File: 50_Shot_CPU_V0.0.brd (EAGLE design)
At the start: 86 x 100 mm, 76 parts, among them IC1 PIC24FJ128GA010, IC2 93LC46ST, J1 J12, J12 A311422_nd, J13 22-23-2021, J14 22-23-2021, J3 22-23-2021, J4 22-23-2021, J5 22-23-2021, Q1 Qs5U34CT-ND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

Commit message: Removed 5V reg and parts
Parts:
- removed C19: 0.01uF, rcl:C0805
- removed C21: 10uF, Mine:CAP3X3
- removed F1: 5A, Mine:SH22,5A
- removed U4: MIC29300, linear:TO263-3
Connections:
- removed net N$60: C21.+, F1.1, U4.3
- removed net VCC: F1.2
- net +12V: no longer C19.1, U4.1
- net GND: no longer C19.2, C21.-, U4.2
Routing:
- net N$60: track 54.7 -> 0.00 mm, vias 1 -> 0
- net VCC: track 37.0 -> 0.00 mm
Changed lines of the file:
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@@
 <attribute name="NAME" x="33.918" y="24.98" size="1.27" layer="25"/>
-</element>
-<element name="C19" library="rcl" package="C0805" value="0.01uF" x="42.178" y="47.836" smashed="yes" rot="R90">
-<attribute name="NAME" x="44.62" y="45.226" size="1.27" layer="25" rot="R180"/>
-</element>
-<element name="C21" library="Mine" package="CAP3X3" value="10uF" x="72.17" y="55.432" smashed="yes" rot="R90">
-<attribute name="NAME" x="73.727" y="52.612" size="1.27" layer="25" rot="R180"/>
 </element>
 <element name="C10" library="rcl" package="C0805" value="10nF" x="57.112" y="48.858" smashed="yes" rot="R180">
@@
 <element name="D3" library="adafruit" package="SOD-123" value="641-1014-6-ND" x="61.38" y="92.82" smashed="yes">
 <attribute name="NAME" x="60.026" y="94.074" size="1.27" layer="25"/>
-</element>
-<element name="F1" library="Mine" package="SH22,5A" value="5A" x="56.368" y="67.79" smashed="yes" rot="R180">
-<attribute name="NAME" x="43.16" y="68.806" size="1.6764" layer="25" ratio="10" rot="R180"/>
-<attribute name="VALUE" x="43.3886" y="65.758" size="1.4224" layer="27" ratio="10" rot="R180"/>
 </element>
 <element name="IC1" library="microchip" package="TQFP100-14X14" value="PIC24FJ128GA010" x="26.79" y="59.89" smashed="yes" rot="R180">
@@
 <attribute name="OC_NEWARK" value="79K3928" x="52.224" y="19.8" size="1.778" layer="27" display="off"/>
 <attribute name="NAME" x="48.5156" y="20.054" size="1.27" layer="25" ratio="10" rot="SR0"/>
-</element>
-<element name="U4" library="linear" package="TO263-3" value="MIC29300" x="66.31" y="34.938" smashed="yes">
-<attribute name="NAME" x="59.804" y="41.926" size="1.27" layer="25" rot="R180"/>
 </element>
 <element name="U1" library="Mine" package="SSOP20" value="MAX6818" x="25.66" y="27.716" smashed="yes" rot="R270">
@@
 <signal name="+12V">
 <contactref element="R1" pad="2"/>
-<contactref element="C19" pad="1"/>
-<contactref element="U4" pad="1"/>
 <contactref element="U2" pad="3"/>
 <contactref element="U2" pad="1"/>
@@
 <wire x1="45.72" y1="46.89" x2="45.71" y2="46.9" width="0.254" layer="1"/>
 <wire x1="45.71" y1="46.9" x2="42.192" y2="46.9" width="0.254" layer="1"/>
-<wire x1="42.192" y1="46.9" x2="42.178" y2="46.886" width="0.254" layer="1"/>
 <wire x1="50.9286" y1="18.8602" x2="49.9738" y2="18.8602" width="0.254" layer="1"/>
 <wire x1="49.9738" y1="18.8602" x2="49.53" y2="19.304" width="0.254" layer="1"/>
@@
 <wire x1="58.674" y1="22.352" x2="53.594" y2="22.352" width="0.254" layer="1"/>
 <wire x1="53.594" y1="22.352" x2="48.006" y2="27.94" width="0.254" layer="1"/>
-<wire x1="63.77" y1="29.1468" x2="63.7068" y2="29.21" width="0.4064" layer="1"/>
 <wire x1="63.7068" y1="29.21" x2="62.23" y2="29.21" width="0.4064" layer="1"/>
 <via x="62.23" y="29.21" extent="1-16" drill="0.6"/>
 <wire x1="46.228" y1="38.354" x2="44.45" y2="38.354" width="0.4064" layer="16"/>
-<wire x1="63.77" y1="29.1468" x2="63.688" y2="29.0648" width="0.254" layer="1"/>
 <wire x1="62.23" y1="29.21" x2="55.372" y2="29.21" width="0.4064" layer="16"/>
 <wire x1="55.372" y1="29.21" x2="46.228" y2="38.354" width="0.4064" layer="16"/>
@@
 <contactref element="C13" pad="2"/>
 <contactref element="C9" pad="2"/>
-<contactref element="C19" pad="2"/>
-<contactref element="C21" pad="-"/>
-<contactref element="U4" pad="2"/>
 <contactref element="U2" pad="2"/>
 <contactref element="U3" pad="2"/>
@@
 <contactref element="IC2" pad="5"/>
 <contactref element="C6" pad="2"/>
-<wire x1="2.064" y1="-46.99" x2="45.546" y2="-51.308" width="0" layer="19" extent="1-1"/>
-<wire x1="13.89" y1="-33.782" x2="2.064" y2="-46.99" width="0" layer="19" extent="1-1"/>
-<wire x1="27.686" y1="-19.05" x2="13.89" y2="-33.782" width="0" layer="19" extent="1-1"/>
-<wire x1="40.64" y1="-18.288" x2="27.686" y2="-19.05" width="0" layer="19" extent="1-1"/>
-<wire x1="52.324" y1="-17.78" x2="40.64" y2="-18.288" width="0" layer="19" extent="1-1"/>
-<wire x1="65.532" y1="-18.288" x2="52.324" y2="-17.78" width="0" layer="19" extent="1-1"/>
-<wire x1="77.216" y1="-18.542" x2="65.532" y2="-18.288" width="0" layer="19" extent="1-1"/>
+<wire x1="65.532" y1="-18.288" x2="77.216" y2="-18.542" width="0" layer="19" extent="1-1"/>
+<wire x1="52.324" y1="-17.78" x2="65.532" y2="-18.288" width="0" layer="19" extent="1-1"/>
+<wire x1="40.64" y1="-18.288" x2="52.324" y2="-17.78" width="0" layer="19" extent="1-1"/>
+<wire x1="27.686" y1="-19.05" x2="40.64" y2="-18.288" width="0" layer="19" extent="1-1"/>
 <wire x1="45.171" y1="-31.873" x2="40.64" y2="-18.288" width="0" layer="19" extent="1-1"/>
 <wire x1="50.988" y1="-35.56" x2="45.171" y2="-31.873" width="0" layer="19" extent="1-1"/>
+<wire x1="45.546" y1="-51.308" x2="50.988" y2="-35.56" width="0" layer="19" extent="1-1"/>
+<wire x1="13.89" y1="-33.782" x2="27.686" y2="-19.05" width="0" layer="19" extent="1-1"/>
+<wire x1="2.064" y1="-46.99" x2="13.89" y2="-33.782" width="0" layer="19" extent="1-1"/>
 <wire x1="80.07" y1="2.78" x2="77.216" y2="-18.542" width="0" layer="19" extent="1-1"/>
-</signal>
-<signal name="VCC">
-<contactref element="F1" pad="2"/>
-<wire x1="80.162" y1="72.39" x2="65.024" y2="72.39" width="0.4064" layer="16"/>
-<wire x1="65.024" y1="72.39" x2="60.424" y2="67.79" width="0.4064" layer="16"/>
-<wire x1="60.424" y1="67.79" x2="45.1158" y2="67.79" width="0.4064" layer="16"/>
 </signal>
 <signal name="VDD">
@@
 <wire x1="43.61" y1="79.932" x2="45.114" y2="79.932" width="0.254" layer="1"/>
 </signal>
-<signal name="N$60">
-<contactref element="C21" pad="+"/>
-<contactref element="U4" pad="3"/>
-<contactref element="F1" pad="1"/>
-<via x="70.866" y="29.21" extent="1-16" drill="0.6"/>
-<wire x1="72.17" y1="56.882" x2="72.136" y2="58.44" width="0.4064" layer="1"/>
-<wire x1="72.136" y1="58.44" x2="72.136" y2="63.2742" width="0.4064" layer="1"/>
-<wire x1="72.136" y1="63.2742" x2="67.6202" y2="67.79" width="0.4064" layer="1"/>
-<wire x1="68.85" y1="29.1468" x2="70.8028" y2="29.1468" width="0.4064" layer="1"/>
-<wire x1="70.8028" y1="29.1468" x2="70.866" y2="29.21" width="0.4064" layer="1"/>
-<wire x1="70.866" y1="29.21" x2="70.866" y2="39.878" width="0.4064" layer="16"/>
-<wire x1="70.866" y1="39.878" x2="67.6202" y2="43.1238" width="0.4064" layer="16"/>
-<wire x1="67.6202" y1="43.1238" x2="67.6202" y2="67.79" width="0.4064" layer="16"/>
-</signal>
 <signal name="ON_LED">

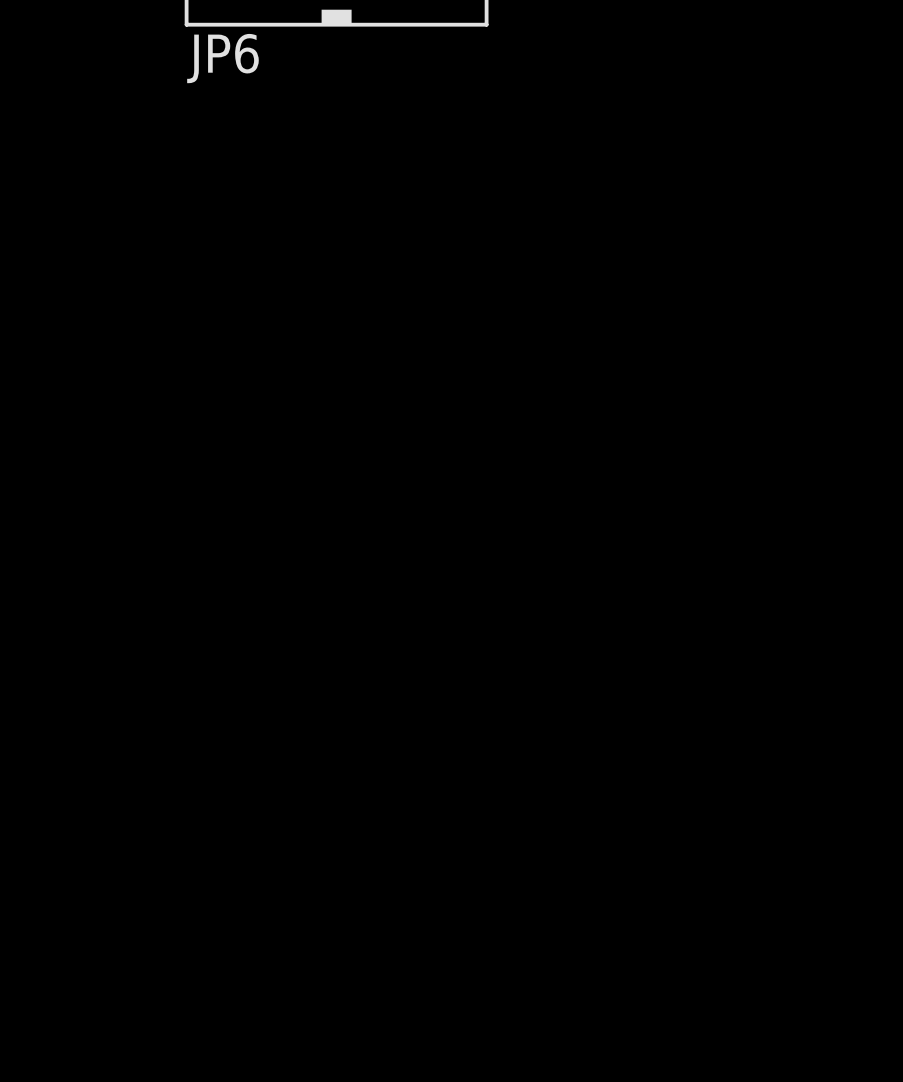
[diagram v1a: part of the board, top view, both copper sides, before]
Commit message: Added parallel display header
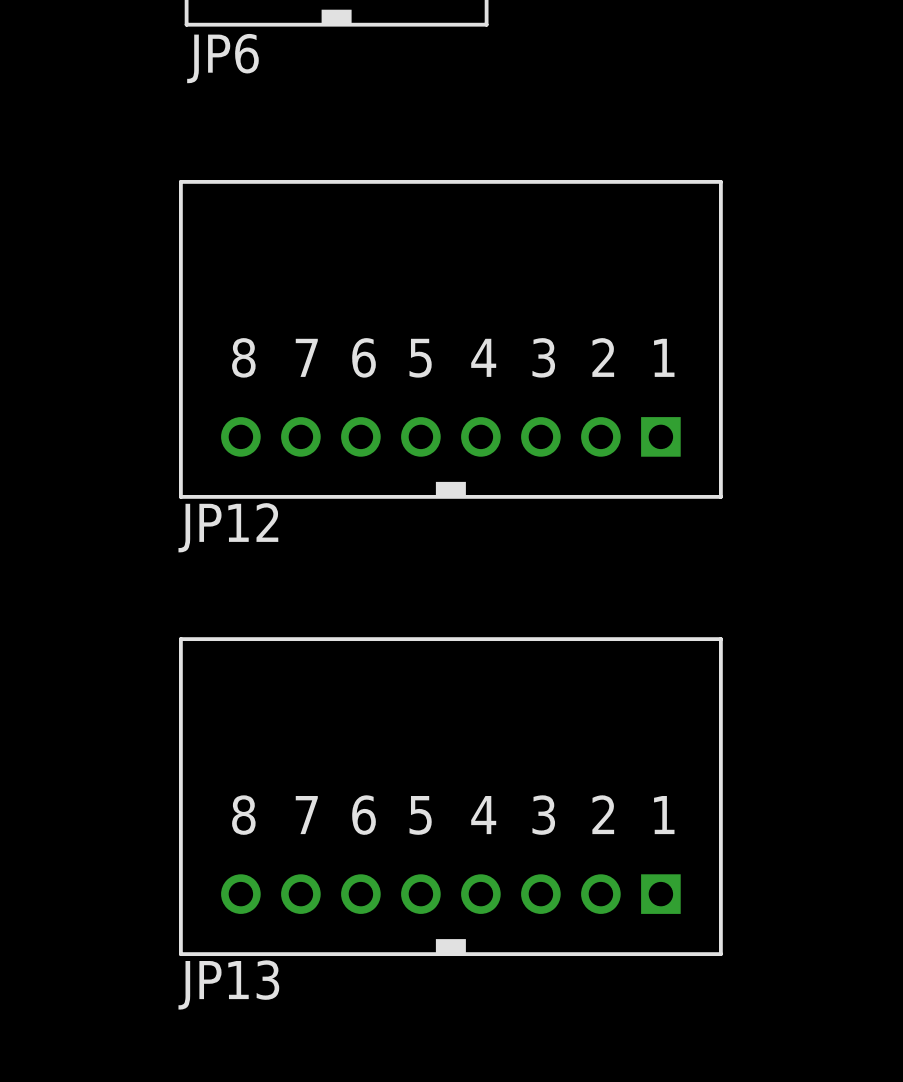
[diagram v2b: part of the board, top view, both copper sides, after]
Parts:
- added JP12, JP13: SHERLOCK_8PIN_RGT, Mine:SHERLOCK_8PIN-RGT
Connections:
- removed net RD10: IC1.70
- removed net RD11: IC1.71
- removed net RD12: IC1.79
- removed net RD13: IC1.80
- removed net RD14: IC1.47
- removed net RD2: IC1.77
- removed net RD3: IC1.78
- removed net RD4: IC1.81
- removed net RD5: IC1.82
- removed net RD6: IC1.83
- removed net RD7: IC1.84
- removed net RD8: IC1.68
- removed net RD9: IC1.69
- new net RD10_CS: IC1.70, JP12.3
- new net RD11_CD: IC1.71, JP12.4
- new net RD12_WR: IC1.79, JP12.5
- new net RD13_RD: IC1.80, JP12.6
- new net RD14_RST: IC1.47, JP12.7
- new net RD2_D0: IC1.77, JP13.1
- new net RD3_D1: IC1.78, JP13.2
- new net RD4_D2: IC1.81, JP13.3
- new net RD5_D3: IC1.82, JP13.4
- new net RD6_D4: IC1.83, JP13.5
- new net RD7_D5: IC1.84, JP13.6
- new net RD8_D6: IC1.68, JP13.7
- new net RD9_D7: IC1.69, JP13.8
- net GND: now also JP12.1
- net RD15: now also JP12.8
- net VDD: now also JP12.2
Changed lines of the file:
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@@
 </element>
 <element name="C6" library="rcl" package="C0805" value=".01uf" x="50.038" y="-35.56"/>
+<element name="JP12" library="Mine" package="SHERLOCK_8PIN-RGT" value="SHERLOCK_8PIN_RGT" x="8.89" y="-107.95"/>
+<element name="JP13" library="Mine" package="SHERLOCK_8PIN-RGT" value="SHERLOCK_8PIN_RGT" x="8.89" y="-123.19"/>
 </elements>
 <signals>
@@
 <contactref element="IC2" pad="5"/>
 <contactref element="C6" pad="2"/>
-<wire x1="65.532" y1="-18.288" x2="77.216" y2="-18.542" width="0" layer="19" extent="1-1"/>
-<wire x1="52.324" y1="-17.78" x2="65.532" y2="-18.288" width="0" layer="19" extent="1-1"/>
-<wire x1="40.64" y1="-18.288" x2="52.324" y2="-17.78" width="0" layer="19" extent="1-1"/>
-<wire x1="27.686" y1="-19.05" x2="40.64" y2="-18.288" width="0" layer="19" extent="1-1"/>
+<contactref element="JP12" pad="1"/>
+<wire x1="2.064" y1="-46.99" x2="15.89" y2="-107.95" width="0" layer="19" extent="1-1"/>
+<wire x1="13.89" y1="-33.782" x2="2.064" y2="-46.99" width="0" layer="19" extent="1-1"/>
+<wire x1="27.686" y1="-19.05" x2="13.89" y2="-33.782" width="0" layer="19" extent="1-1"/>
+<wire x1="40.64" y1="-18.288" x2="27.686" y2="-19.05" width="0" layer="19" extent="1-1"/>
+<wire x1="52.324" y1="-17.78" x2="40.64" y2="-18.288" width="0" layer="19" extent="1-1"/>
+<wire x1="65.532" y1="-18.288" x2="52.324" y2="-17.78" width="0" layer="19" extent="1-1"/>
+<wire x1="77.216" y1="-18.542" x2="65.532" y2="-18.288" width="0" layer="19" extent="1-1"/>
 <wire x1="45.171" y1="-31.873" x2="40.64" y2="-18.288" width="0" layer="19" extent="1-1"/>
 <wire x1="50.988" y1="-35.56" x2="45.171" y2="-31.873" width="0" layer="19" extent="1-1"/>
 <wire x1="45.546" y1="-51.308" x2="50.988" y2="-35.56" width="0" layer="19" extent="1-1"/>
-<wire x1="13.89" y1="-33.782" x2="27.686" y2="-19.05" width="0" layer="19" extent="1-1"/>
-<wire x1="2.064" y1="-46.99" x2="13.89" y2="-33.782" width="0" layer="19" extent="1-1"/>
 <wire x1="80.07" y1="2.78" x2="77.216" y2="-18.542" width="0" layer="19" extent="1-1"/>
 </signal>
@@
 <contactref element="IC2" pad="8"/>
 <contactref element="C6" pad="1"/>
+<contactref element="JP12" pad="2"/>
 <wire x1="32.29" y1="72.31" x2="32.31" y2="72.33" width="0" layer="19" extent="1-1"/>
 <wire x1="54.356" y1="24.13" x2="53.5194" y2="21.4106" width="0" layer="19" extent="1-1"/>
@@
 <wire x1="43.221" y1="-31.873" x2="17.018" y2="7.112" width="0" layer="19" extent="1-1"/>
 <wire x1="49.088" y1="-35.56" x2="43.221" y2="-31.873" width="0" layer="19" extent="1-1"/>
-<wire x1="43.546" y1="-51.308" x2="43.221" y2="-31.873" width="0" layer="19" extent="1-1"/>
+<wire x1="43.546" y1="-51.308" x2="49.088" y2="-35.56" width="0" layer="19" extent="1-1"/>
+<wire x1="13.89" y1="-107.95" x2="43.546" y2="-51.308" width="0" layer="19" extent="1-1"/>
 </signal>
 <signal name="SM_LED">
@@
 <signal name="RD15">
 <contactref element="IC1" pad="48"/>
-</signal>
-<signal name="RD14">
+<contactref element="JP12" pad="8"/>
+<wire x1="19.04" y1="54.89" x2="1.89" y2="-107.95" width="0" layer="19" extent="1-1"/>
+</signal>
+<signal name="RD14_RST">
 <contactref element="IC1" pad="47"/>
+<contactref element="JP12" pad="7"/>
+<wire x1="19.04" y1="55.39" x2="3.89" y2="-107.95" width="0" layer="19" extent="1-1"/>
 </signal>
 <signal name="RD1">
 <contactref element="IC1" pad="76"/>
 </signal>
-<signal name="RD2">
+<signal name="RD2_D0">
 <contactref element="IC1" pad="77"/>
-</signal>
-<signal name="RD3">
+<contactref element="JP13" pad="1"/>
+<wire x1="34.54" y1="54.39" x2="15.89" y2="-123.19" width="0" layer="19" extent="1-1"/>
+</signal>
+<signal name="RD3_D1">
 <contactref element="IC1" pad="78"/>
-</signal>
-<signal name="RD12">
+<contactref element="JP13" pad="2"/>
+<wire x1="34.54" y1="54.89" x2="13.89" y2="-123.19" width="0" layer="19" extent="1-1"/>
+</signal>
+<signal name="RD12_WR">
 <contactref element="IC1" pad="79"/>
-</signal>
-<signal name="RD13">
+<contactref element="JP12" pad="5"/>
+<wire x1="34.54" y1="55.39" x2="7.89" y2="-107.95" width="0" layer="19" extent="1-1"/>
+</signal>
+<signal name="RD13_RD">
 <contactref element="IC1" pad="80"/>
-</signal>
-<signal name="RD4">
+<contactref element="JP12" pad="6"/>
+<wire x1="34.54" y1="55.89" x2="5.89" y2="-107.95" width="0" layer="19" extent="1-1"/>
+</signal>
+<signal name="RD4_D2">
 <contactref element="IC1" pad="81"/>
-</signal>
-<signal name="RD5">
+<contactref element="JP13" pad="3"/>
+<wire x1="34.54" y1="56.39" x2="11.89" y2="-123.19" width="0" layer="19" extent="1-1"/>
+</signal>
+<signal name="RD5_D3">
 <contactref element="IC1" pad="82"/>
-</signal>
-<signal name="RD6">
+<contactref element="JP13" pad="4"/>
+<wire x1="34.54" y1="56.89" x2="9.89" y2="-123.19" width="0" layer="19" extent="1-1"/>
+</signal>
+<signal name="RD6_D4">
 <contactref element="IC1" pad="83"/>
-</signal>
-<signal name="RD7">
+<contactref element="JP13" pad="5"/>
+<wire x1="34.54" y1="57.39" x2="7.89" y2="-123.19" width="0" layer="19" extent="1-1"/>
+</signal>
+<signal name="RD7_D5">
 <contactref element="IC1" pad="84"/>
-</signal>
-<signal name="RD8">
+<contactref element="JP13" pad="6"/>
+<wire x1="34.54" y1="57.89" x2="5.89" y2="-123.19" width="0" layer="19" extent="1-1"/>
+</signal>
+<signal name="RD8_D6">
 <contactref element="IC1" pad="68"/>
-</signal>
-<signal name="RD9">
+<contactref element="JP13" pad="7"/>
+<wire x1="29.29" y1="52.14" x2="3.89" y2="-123.19" width="0" layer="19" extent="1-1"/>
+</signal>
+<signal name="RD9_D7">
 <contactref element="IC1" pad="69"/>
-</signal>
-<signal name="RD10">
+<contactref element="JP13" pad="8"/>
+<wire x1="29.79" y1="52.14" x2="1.89" y2="-123.19" width="0" layer="19" extent="1-1"/>
+</signal>
+<signal name="RD10_CS">
 <contactref element="IC1" pad="70"/>
+<contactref element="JP12" pad="3"/>
+<wire x1="30.29" y1="52.14" x2="11.89" y2="-107.95" width="0" layer="19" extent="1-1"/>
 </signal>
 <signal name="RD0">
 <contactref element="IC1" pad="72"/>
 </signal>
-<signal name="RD11">
+<signal name="RD11_CD">
 <contactref element="IC1" pad="71"/>
+<contactref element="JP12" pad="4"/>
+<wire x1="30.79" y1="52.14" x2="9.89" y2="-107.95" width="0" layer="19" extent="1-1"/>
 </signal>
 <signal name="ARM_RELAY">

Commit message: Added UART Header
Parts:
- added JP14: SHERLOCK_6PIN_RGT, Mine:SHERLOCK_6PIN_RGT
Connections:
- new net RF12_U2CTS: IC1.40, JP14.6
- new net RF13_U2RTS: IC1.39, JP14.5
- new net RF4_U2RX: IC1.49, JP14.3
- new net RF5_U2TX: IC1.50, JP14.4
- net GND: now also JP14.2
- net VDD: now also JP14.1
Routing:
- net RB12_X+: track 42.7 -> 0.00 mm
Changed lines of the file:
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@@
 <element name="JP12" library="Mine" package="SHERLOCK_8PIN-RGT" value="SHERLOCK_8PIN_RGT" x="8.89" y="-107.95"/>
 <element name="JP13" library="Mine" package="SHERLOCK_8PIN-RGT" value="SHERLOCK_8PIN_RGT" x="8.89" y="-123.19"/>
+<element name="JP14" library="Mine" package="SHERLOCK_6PIN_RGT" value="SHERLOCK_6PIN_RGT" x="7.112" y="-136.398"/>
 </elements>
 <signals>
@@
 <contactref element="C6" pad="2"/>
 <contactref element="JP12" pad="1"/>
+<contactref element="JP14" pad="2"/>
+<wire x1="15.89" y1="-107.95" x2="10.112" y2="-136.398" width="0" layer="19" extent="1-1"/>
 <wire x1="2.064" y1="-46.99" x2="15.89" y2="-107.95" width="0" layer="19" extent="1-1"/>
 <wire x1="13.89" y1="-33.782" x2="2.064" y2="-46.99" width="0" layer="19" extent="1-1"/>
@@
 <contactref element="C6" pad="1"/>
 <contactref element="JP12" pad="2"/>
-<wire x1="32.29" y1="72.31" x2="32.31" y2="72.33" width="0" layer="19" extent="1-1"/>
+<contactref element="JP14" pad="1"/>
+<wire x1="13.89" y1="-107.95" x2="12.112" y2="-136.398" width="0" layer="19" extent="1-1"/>
+<wire x1="43.546" y1="-51.308" x2="13.89" y2="-107.95" width="0" layer="19" extent="1-1"/>
+<wire x1="49.088" y1="-35.56" x2="43.546" y2="-51.308" width="0" layer="19" extent="1-1"/>
+<wire x1="43.221" y1="-31.873" x2="49.088" y2="-35.56" width="0" layer="19" extent="1-1"/>
+<wire x1="17.018" y1="7.112" x2="43.221" y2="-31.873" width="0" layer="19" extent="1-1"/>
+<wire x1="32.31" y1="72.33" x2="32.29" y2="72.31" width="0" layer="19" extent="1-1"/>
 <wire x1="54.356" y1="24.13" x2="53.5194" y2="21.4106" width="0" layer="19" extent="1-1"/>
 <wire x1="5.842" y1="63.212" x2="10.414" y2="63.754" width="0" layer="19" extent="1-16"/>
 <wire x1="-1.59" y1="-9.144" x2="15.756" y2="7.052" width="0" layer="19" extent="1-1"/>
-<wire x1="43.221" y1="-31.873" x2="17.018" y2="7.112" width="0" layer="19" extent="1-1"/>
-<wire x1="49.088" y1="-35.56" x2="43.221" y2="-31.873" width="0" layer="19" extent="1-1"/>
-<wire x1="43.546" y1="-51.308" x2="49.088" y2="-35.56" width="0" layer="19" extent="1-1"/>
-<wire x1="13.89" y1="-107.95" x2="43.546" y2="-51.308" width="0" layer="19" extent="1-1"/>
 </signal>
 <signal name="SM_LED">
@@
 <contactref element="JP1" pad="1"/>
 <contactref element="IC1" pad="41"/>
-<wire x1="19.04" y1="58.39" x2="16.794" y2="58.39" width="0.254" layer="1"/>
-<wire x1="16.794" y1="58.39" x2="15.494" y2="59.69" width="0.254" layer="1"/>
-<wire x1="15.494" y1="59.69" x2="15.494" y2="71.882" width="0.254" layer="1"/>
-<wire x1="15.494" y1="71.882" x2="26.924" y2="83.312" width="0.254" layer="1"/>
-<wire x1="26.924" y1="83.312" x2="26.924" y2="88.9" width="0.254" layer="1"/>
-<wire x1="26.924" y1="88.9" x2="23.652" y2="92.172" width="0.254" layer="1"/>
-<wire x1="8.08" y1="-20.574" x2="16.794" y2="58.39" width="0" layer="19" extent="1-1"/>
+<wire x1="8.08" y1="-20.574" x2="19.04" y2="58.39" width="0" layer="19" extent="1-1"/>
 </signal>
 <signal name="RF2_X-">
@@
 <wire x1="44.521" y1="-31.873" x2="32.79" y2="67.64" width="0" layer="19" extent="1-1"/>
 </signal>
+<signal name="RF13_U2RTS">
+<contactref element="JP14" pad="5"/>
+<contactref element="IC1" pad="39"/>
+<wire x1="19.04" y1="59.39" x2="4.112" y2="-136.398" width="0" layer="19" extent="1-1"/>
+</signal>
+<signal name="RF12_U2CTS">
+<contactref element="JP14" pad="6"/>
+<contactref element="IC1" pad="40"/>
+<wire x1="19.04" y1="58.89" x2="2.112" y2="-136.398" width="0" layer="19" extent="1-1"/>
+</signal>
+<signal name="RF5_U2TX">
+<contactref element="IC1" pad="50"/>
+<contactref element="JP14" pad="4"/>
+<wire x1="19.04" y1="53.89" x2="6.112" y2="-136.398" width="0" layer="19" extent="1-1"/>
+</signal>
+<signal name="RF4_U2RX">
+<contactref element="IC1" pad="49"/>
+<contactref element="JP14" pad="3"/>
+<wire x1="19.04" y1="54.39" x2="8.112" y2="-136.398" width="0" layer="19" extent="1-1"/>
+</signal>
 </signals>
